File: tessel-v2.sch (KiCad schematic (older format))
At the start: 0 parts

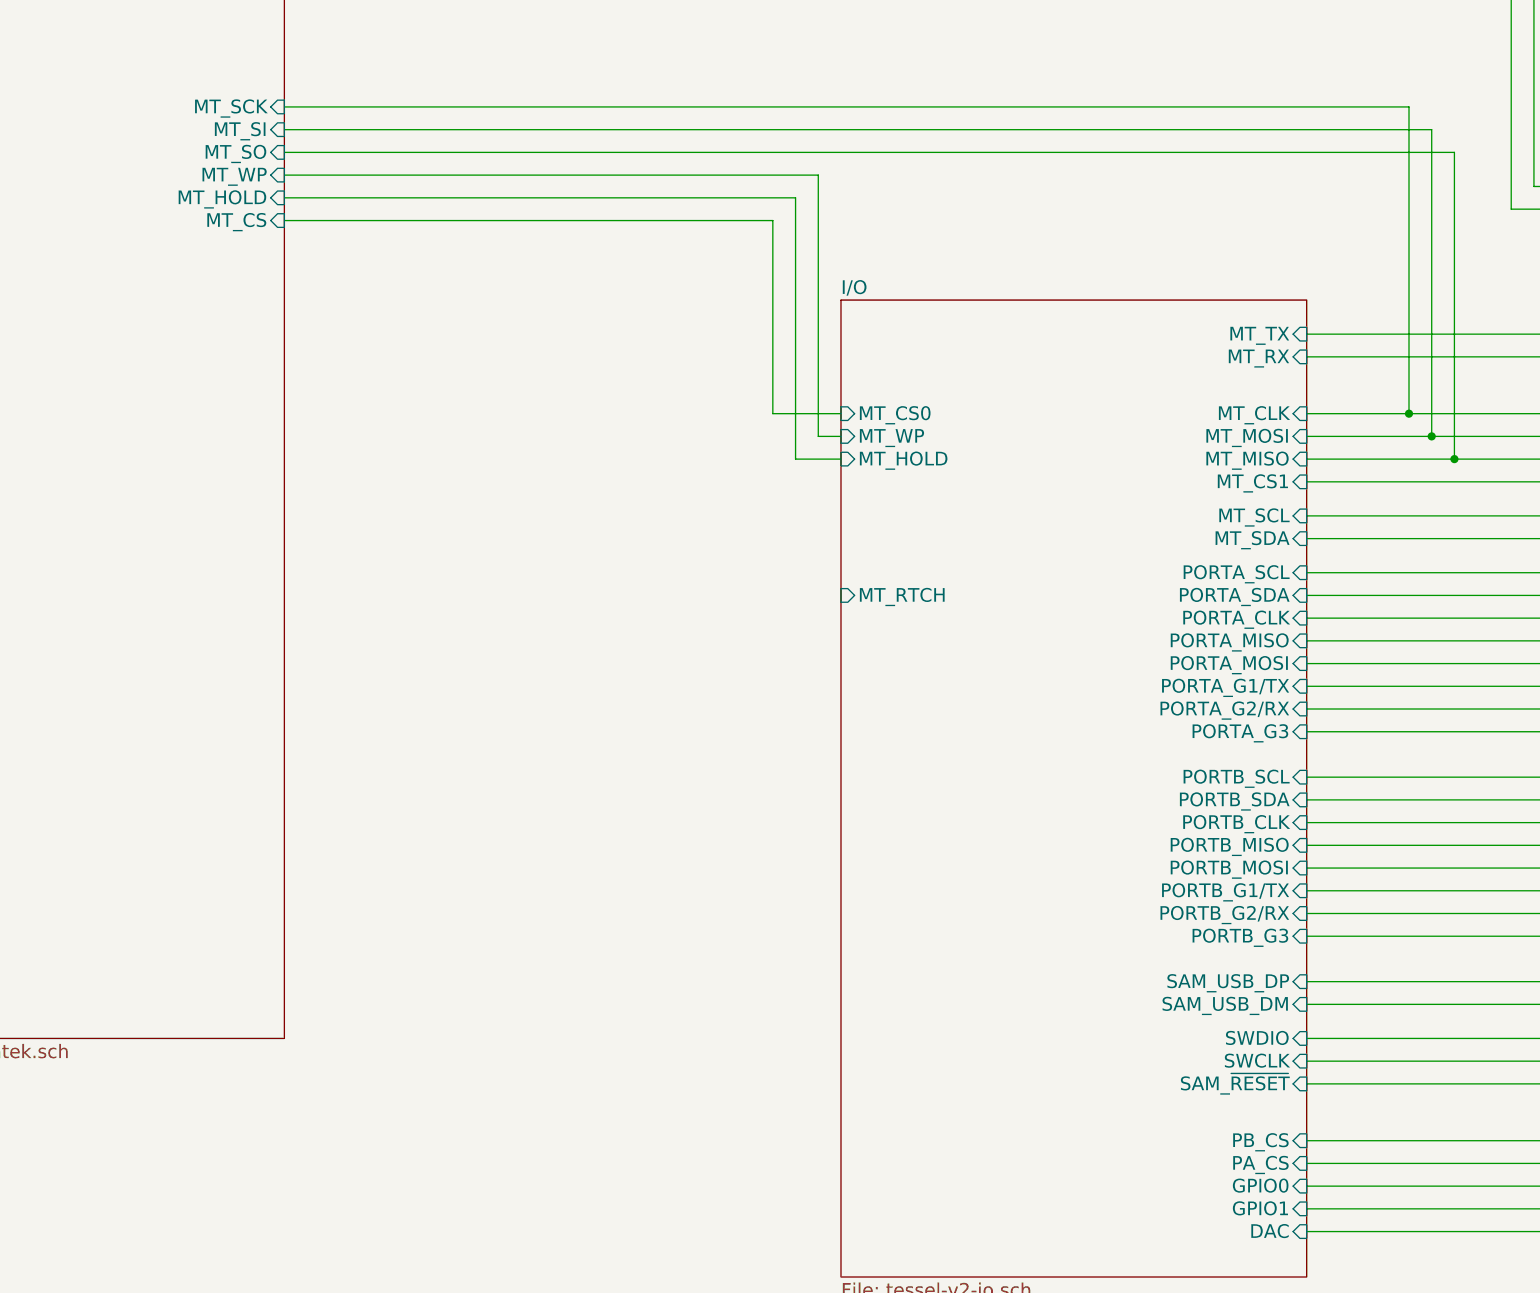
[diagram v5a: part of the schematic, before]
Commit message: added boot configs for mediatek
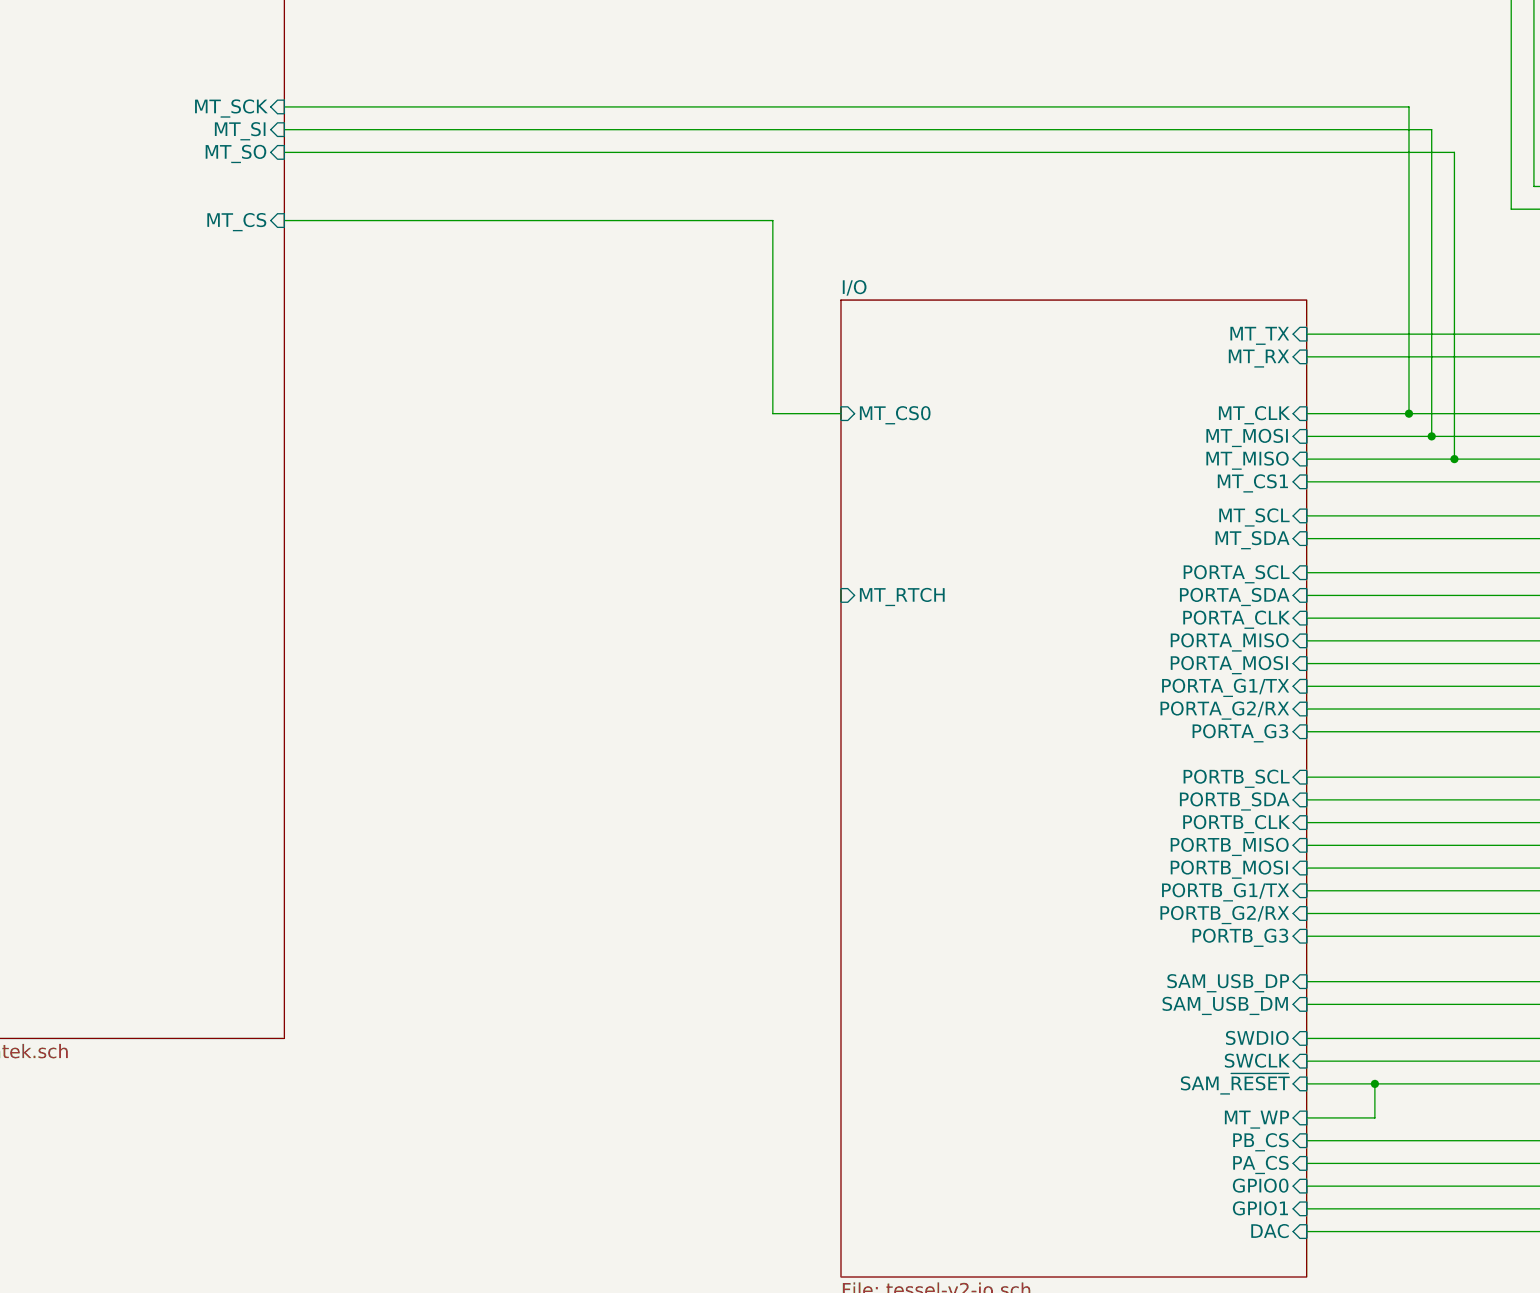
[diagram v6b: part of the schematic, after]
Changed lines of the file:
@@
 F3 "MT_SI" I R 4500 4250 60
 F4 "MT_SO" I R 4500 4350 60
-F5 "MT_WP" I R 4500 4450 60
-F6 "MT_HOLD" I R 4500 4550 60
 F7 "MT_CS" I R 4500 4650 60
 F8 "MT_SCK" I R 4500 4150 60
@@
 	9650 4350 9650 5700
 Connection ~ 9650 5700
-Wire Wire Line
-	4500 4450 6850 4450
-Wire Wire Line
-	6850 4450 6850 5600
-Wire Wire Line
-	6850 5600 6950 5600
-Wire Wire Line
-	4500 4550 6750 4550
-Wire Wire Line
-	6750 4550 6750 5700
-Wire Wire Line
-	6750 5700 6950 5700
 Wire Wire Line
 	4500 4650 6650 4650
@@
 F7 "MT_MOSI" I R 9000 5600 60
 F8 "MT_MISO" I R 9000 5700 60
-F9 "MT_WP" I L 6950 5600 60
-F10 "MT_HOLD" I L 6950 5700 60
+F9 "MT_WP" I R 9000 8600 60
 F11 "MT_SCL" I R 9000 5950 60
 F12 "MT_SDA" I R 9000 6050 60
@@
 Wire Wire Line
 	13150 7450 13050 7450
+Wire Wire Line
+	9000 8600 9300 8600
+Wire Wire Line
+	9300 8600 9300 8450
+Connection ~ 9300 8450
 $EndSCHEMATC

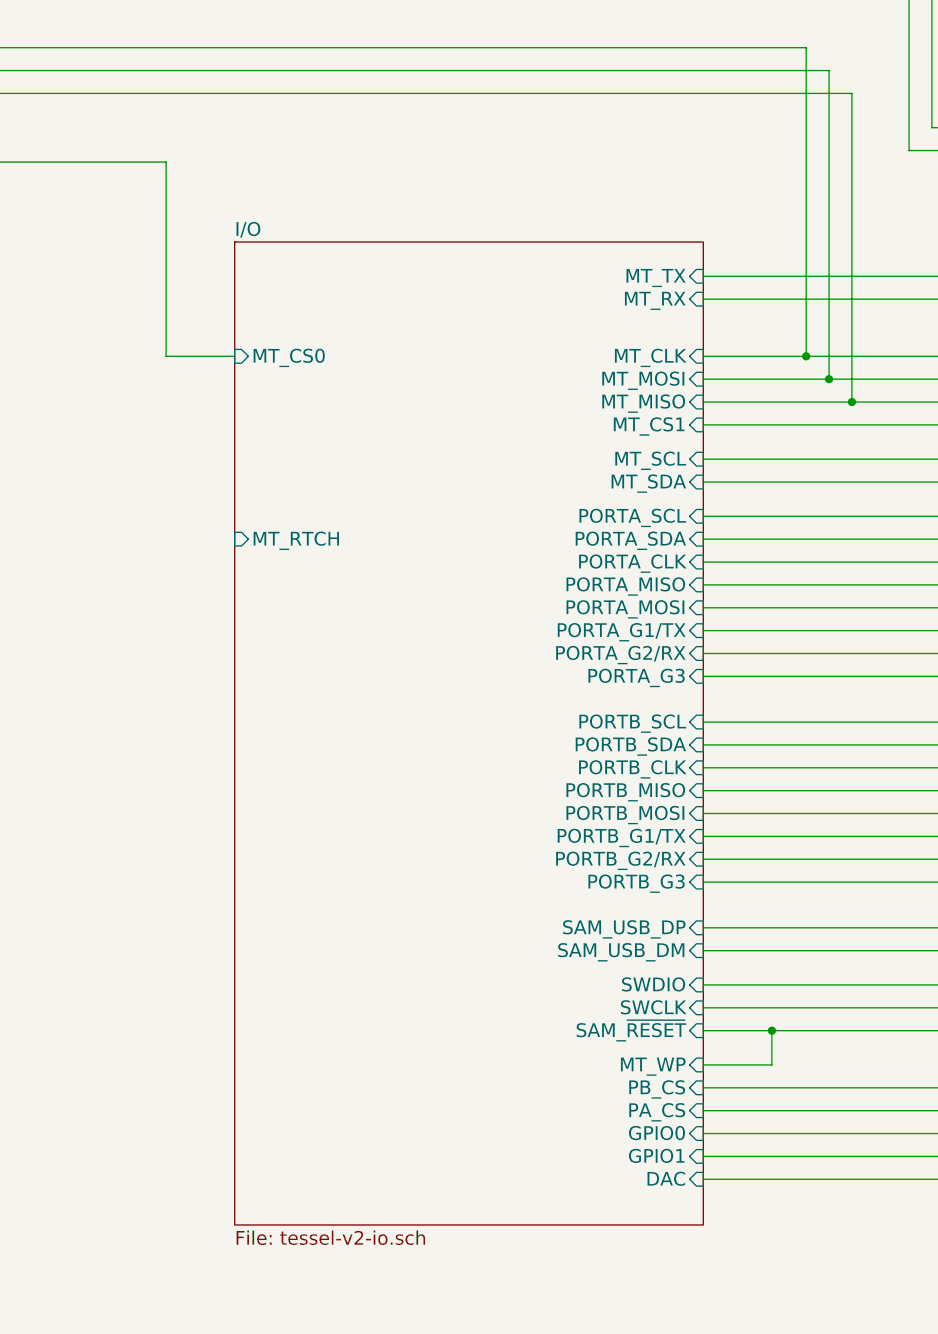
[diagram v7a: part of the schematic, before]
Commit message: wiring gpio0_1 to cs0
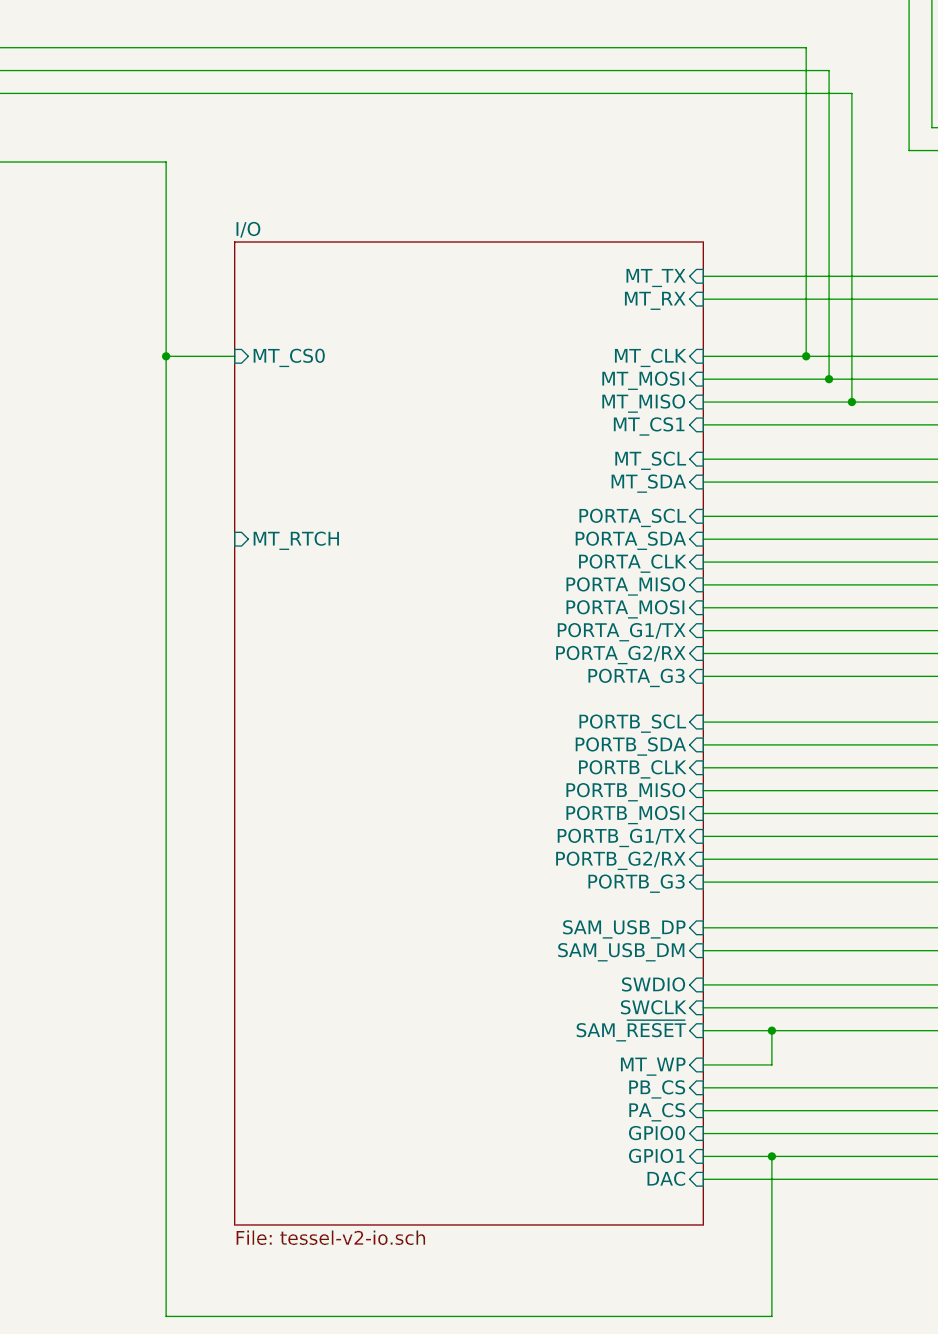
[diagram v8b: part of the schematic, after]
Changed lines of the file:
@@
 	4500 4650 6650 4650
 Wire Wire Line
-	6650 4650 6650 5500
+	6650 4650 6650 9700
 Wire Wire Line
 	6650 5500 6950 5500
@@
 	9300 8600 9300 8450
 Connection ~ 9300 8450
+Wire Wire Line
+	9300 9000 9300 9700
+Wire Wire Line
+	9300 9700 6650 9700
+Connection ~ 6650 5500
+Connection ~ 9300 9000
 $EndSCHEMATC
